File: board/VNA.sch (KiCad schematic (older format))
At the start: 85 parts, among them J1 Conn_02x07_Odd_Even, J10 Conn_01x01, J11 Conn_01x01, J12 Conn_01x01, J13 Barrel_Jack, J16 USB_B, J17 Conn_01x04, J18 Conn_01x01, J19 Conn_01x01, J2 Conn_Coaxial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

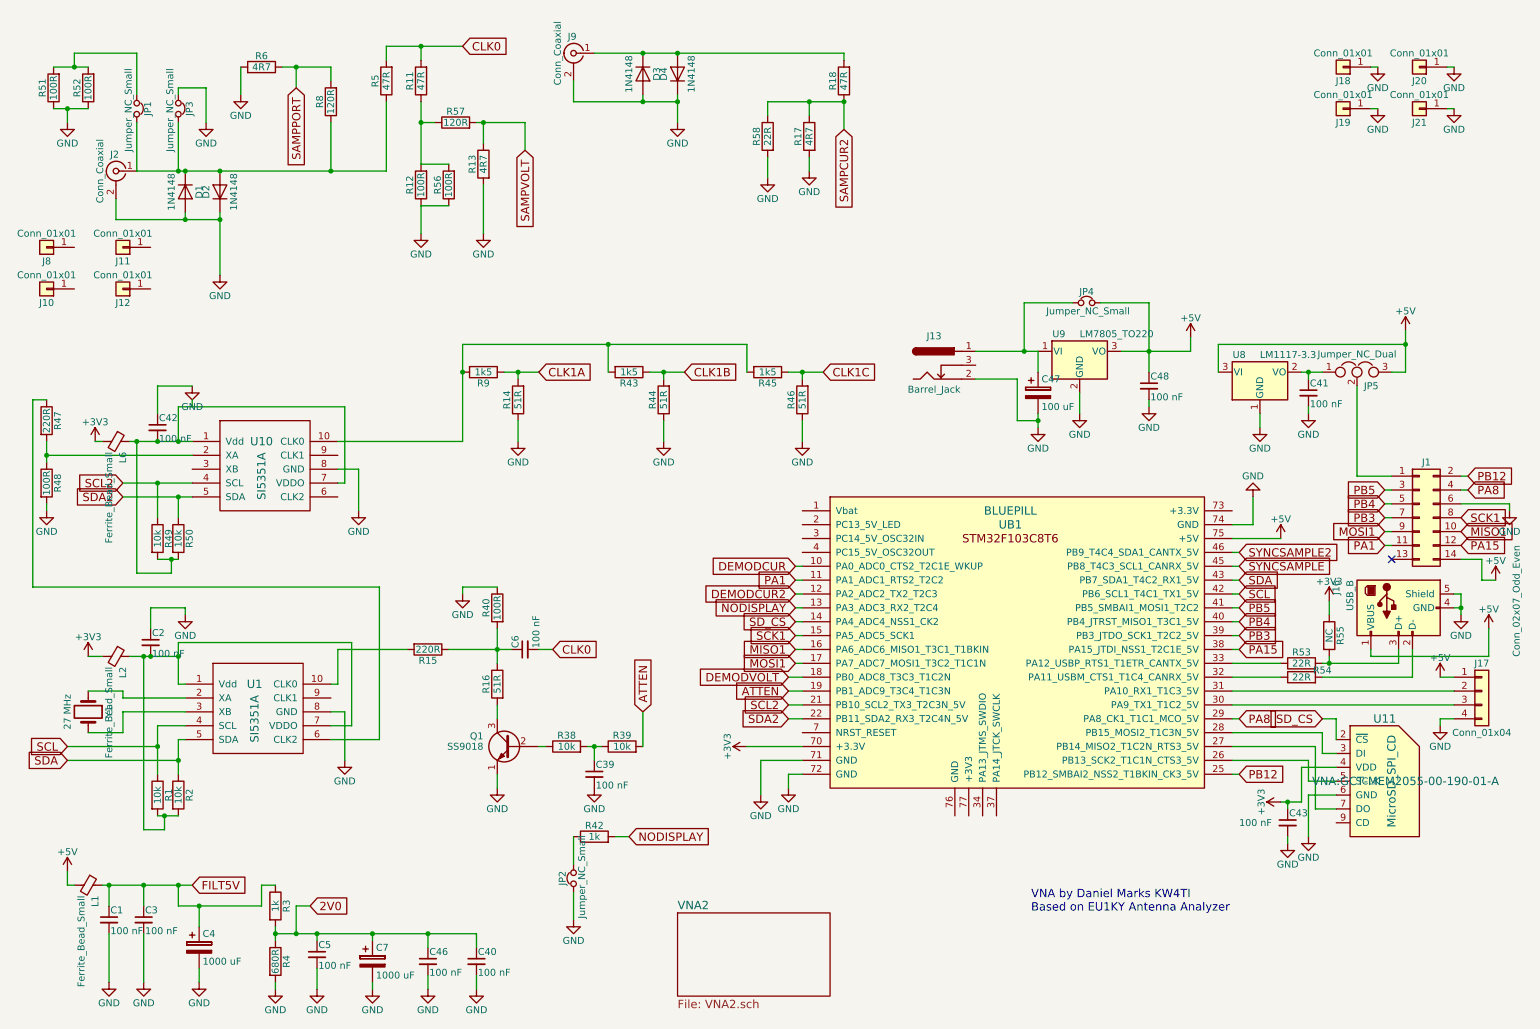
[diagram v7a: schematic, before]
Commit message: Modified some component values on bridge for better performance
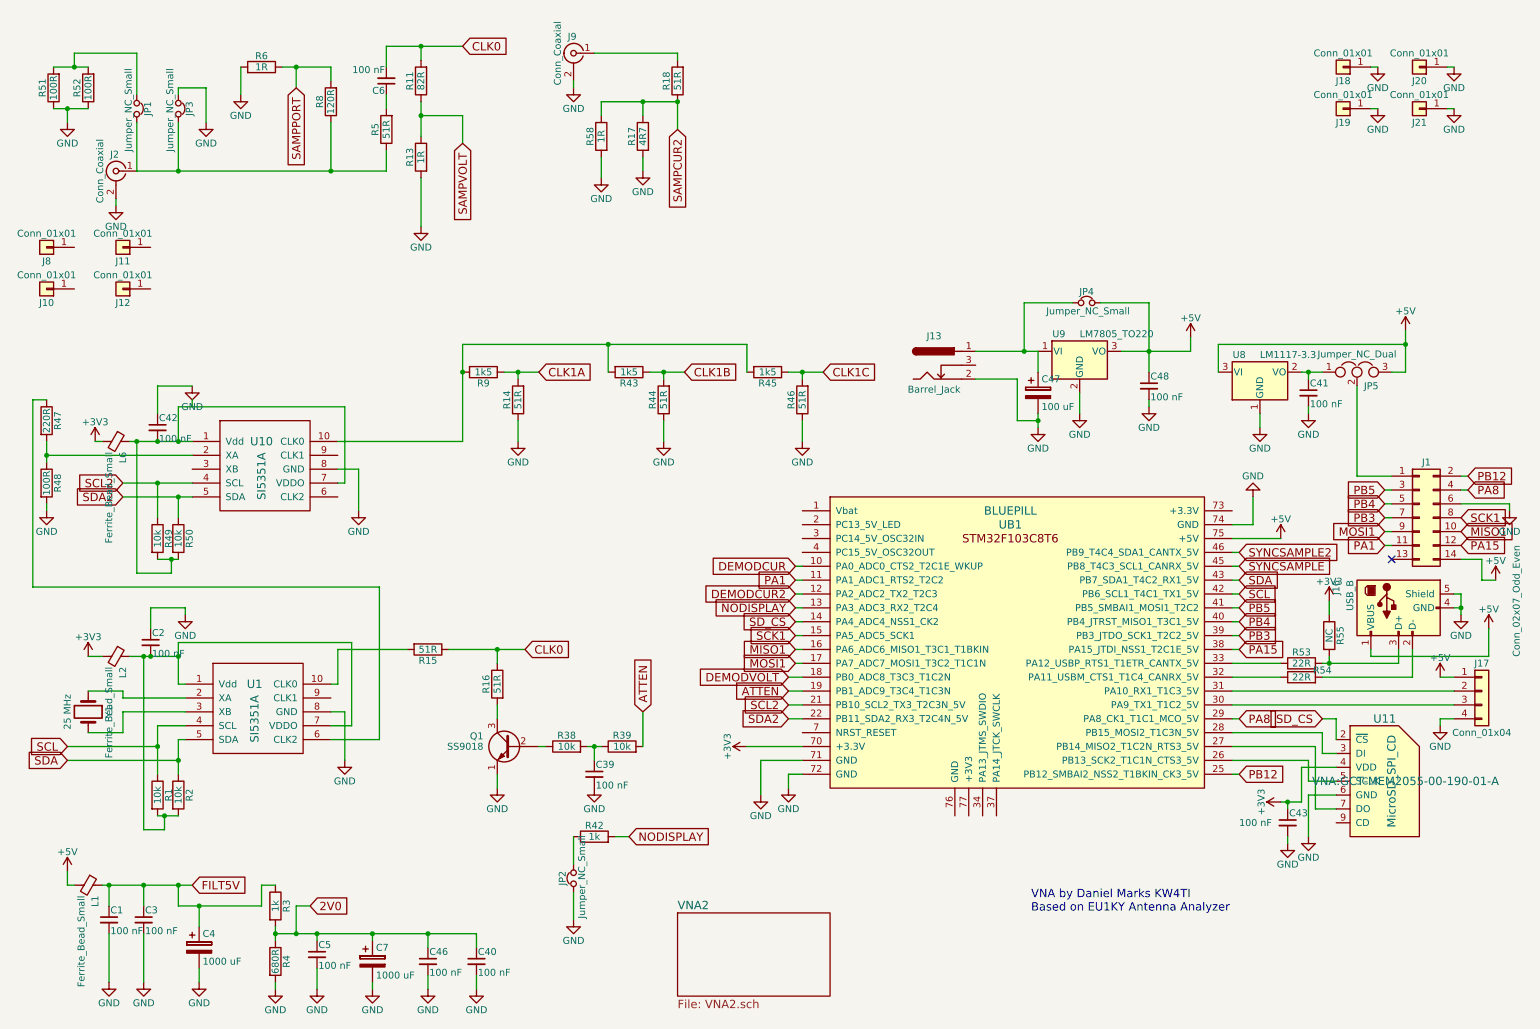
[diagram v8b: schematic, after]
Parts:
- removed D1, D2, D3, D4: 1N4148, Diodes_THT:D_DO-35_SOD27_P7.62mm_Horizontal, symbol D
- removed R12, R40, R56: 100R, Resistors_THT:R_Axial_DIN0207_L6.3mm_D2.5mm_P7.62mm_Horizontal, symbol R
- removed R57: 120R, Resistors_THT:R_Axial_DIN0207_L6.3mm_D2.5mm_P7.62mm_Horizontal, symbol R
- R11: value 47R -> 82R
- R13, R6: value 4R7 -> 1R
- R15: value 220R -> 51R
- R18, R5: value 47R -> 51R
- R58: value 22R -> 1R
- Y1: value 27 MHz -> 25 MHz
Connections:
- net CLK0: now also R15.1, R16.1; no longer R5.2
- net SAMPVOLT: now also R11.1
- new net: C6.1, R5.2
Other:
- moved on the sheet: C6, R13, R17, R18, R5, R58
